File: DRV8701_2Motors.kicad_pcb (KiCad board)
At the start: 4 copper layers, 100 x 40 mm, 99 parts, among them J1 Conn_01x02, J12 Conn_01x02, J13 Conn_01x02, J2 Conn_01x10, J3 Conn_01x10, J6 Conn_01x04, J7 Conn_ST_STDC14, J8 Conn_01x04, J9 Conn_01x04, SW1 SW_SPDT_321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

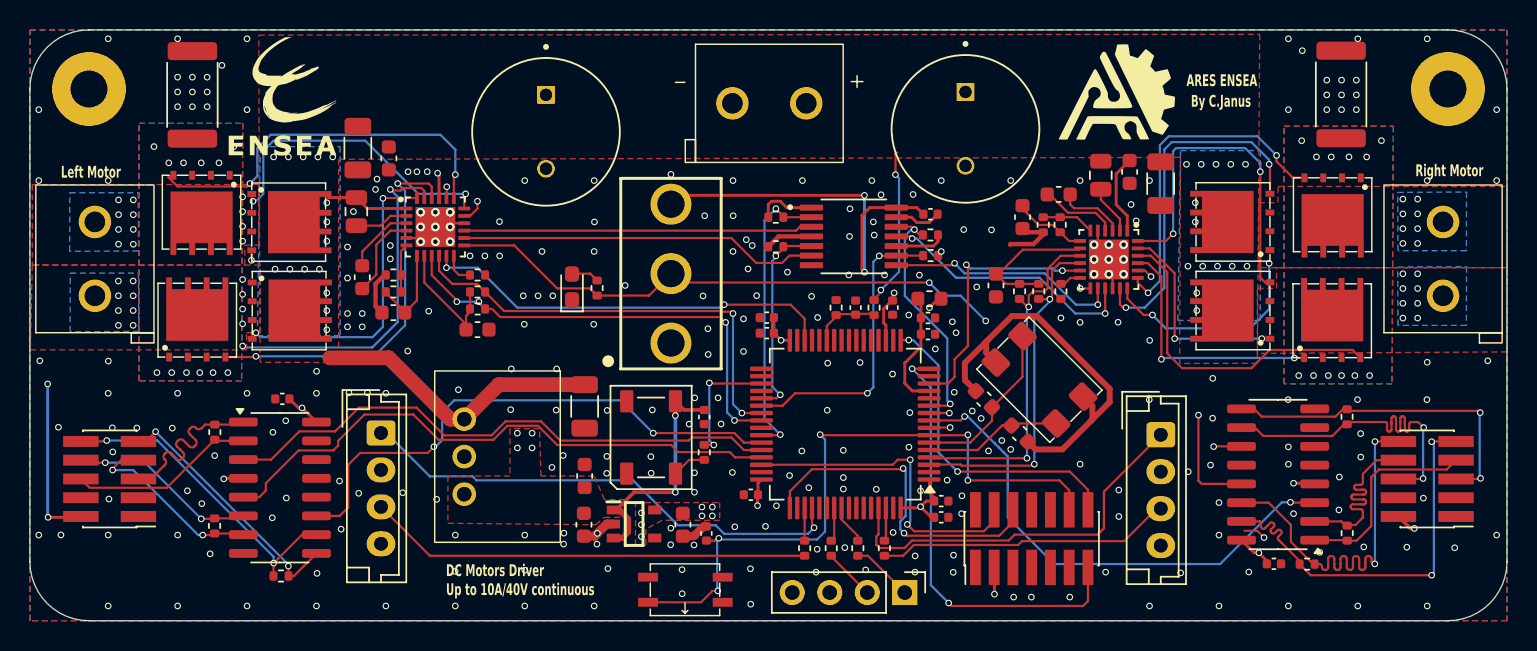
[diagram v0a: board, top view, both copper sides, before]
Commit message: alignement connecteur, changement connecteur
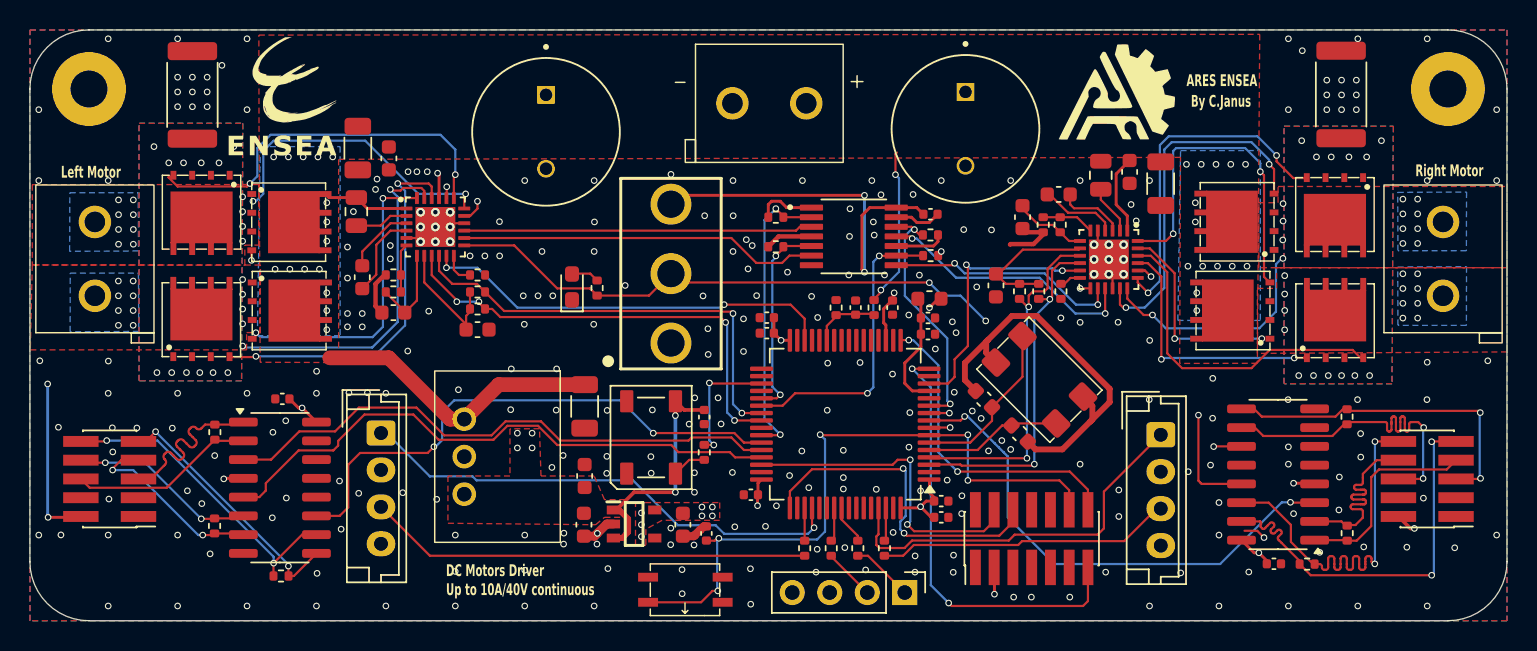
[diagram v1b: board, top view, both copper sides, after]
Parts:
- moved U21 0.28 mm to (85.6, 84.3)
- moved U24 0.28 mm to (155.4, 78.0)
- moved U20 0.20 mm to (162.4, 84.3)
- moved U22 0.16 mm to (162.3, 77.8)
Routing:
- net /MoteurDroit/SH1: track 14.8 -> 15.9 mm, vias 10 -> 13
- net /MoteurDroit/SH2: vias 10 -> 14
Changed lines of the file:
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@@
 	(footprint "TPH1R403NL:TPH1R403NL"
 		(layer "F.Cu")
-		(at 155.1 78 -90)
+		(at 155.38 77.99 -90)
 		(property "Reference" "U24"
 			(at -0.035 -6 270)
@@
 	(footprint "TPH1R403NL:TPH1R403NL"
 		(layer "F.Cu")
-		(at 85.33 84.3 180)
+		(at 85.61 84.27 180)
 		(property "Reference" "U21"
 			(at -0.035 -6 180)
@@
 	(footprint "TPH1R403NL:TPH1R403NL"
 		(layer "F.Cu")
-		(at 162.195 77.865)
+		(at 162.35 77.85)
 		(property "Reference" "U22"
 			(at -0.035 -6 0)
@@
 	(footprint "TPH1R403NL:TPH1R403NL"
 		(layer "F.Cu")
-		(at 162.165 84.34 180)
+		(at 162.36 84.34 180)
 		(property "Reference" "U20"
 			(at -0.035 -6 180)
@@
 	)
 	(segment
-		(start 157.3 81.77)
-		(end 157.625 82.095)
+		(start 151.4 78.8)
+		(end 150.91 79.29)
 		(width 0.15)
 		(layer "F.Cu")
@@
 	)
 	(segment
-		(start 157.625 82.095)
-		(end 157.95 82.095)
+		(start 157.3 74.6)
+		(end 157.55 74.85)
 		(width 0.15)
 		(layer "F.Cu")
@@
 	)
 	(segment
-		(start 151.4 78.8)
-		(end 150.91 79.29)
+		(start 157.55 74.85)
+		(end 157.55 81.72)
 		(width 0.15)
 		(layer "F.Cu")
@@
 	)
 	(segment
-		(start 157.3 74.6)
-		(end 157.3 81.77)
+		(start 157.925 82.095)
+		(end 157.95 82.095)
+		(width 0.15)
+		(layer "F.Cu")
+		(net 108)
+	)
+	(segment
+		(start 157.55 81.72)
+		(end 157.925 82.095)
 		(width 0.15)
 		(layer "F.Cu")
@@
 	)
 	(segment
-		(start 149.89 80.29)
-		(end 149 80.29)
+		(start 152 87.9)
+		(end 151 86.9)
 		(width 0.15)
 		(layer "F.Cu")
@@
 	)
 	(segment
-		(start 152 87.9)
-		(end 151 86.9)
+		(start 156.7 87.9)
+		(end 152 87.9)
 		(width 0.15)
 		(layer "F.Cu")
@@
 	)
 	(segment
+		(start 151 81.4)
+		(end 149.89 80.29)
+		(width 0.15)
+		(layer "F.Cu")
+		(net 109)
+	)
+	(segment
 		(start 163.544 86.664)
 		(end 157.936 86.664)
@@
 	)
 	(segment
-		(start 156.7 87.9)
-		(end 152 87.9)
+		(start 149.89 80.29)
+		(end 149 80.29)
 		(width 0.15)
 		(layer "F.Cu")
@@
 	)
 	(segment
-		(start 151 81.4)
-		(end 149.89 80.29)
+		(start 164.07 87.19)
+		(end 163.544 86.664)
 		(width 0.15)
 		(layer "F.Cu")
@@
 	)
 	(segment
-		(start 164.07 87.19)
-		(end 163.544 86.664)
+		(start 164.265 87.19)
+		(end 164.07 87.19)
 		(width 0.15)
 		(layer "F.Cu")
@@
 	)
 	(segment
+		(start 89.25 87.15)
+		(end 87.545 87.15)
+		(width 0.15)
+		(layer "F.Cu")
+		(net 110)
+	)
+	(segment
 		(start 101 75.4)
 		(end 101.2 75.6)
@@
 	)
 	(segment
-		(start 101.2 75.6)
-		(end 101.2 76.385)
+		(start 87.545 87.15)
+		(end 87.515 87.12)
 		(width 0.15)
 		(layer "F.Cu")
@@
 	)
 	(segment
-		(start 98.9 75.4)
-		(end 101 75.4)
+		(start 101.2 75.6)
+		(end 101.2 76.385)
 		(width 0.15)
 		(layer "F.Cu")
@@
 	)
 	(segment
-		(start 89.25 87.15)
-		(end 87.235 87.15)
+		(start 98.9 75.4)
+		(end 101 75.4)
 		(width 0.15)
 		(layer "F.Cu")
@@
 	)
 	(via
+		(at 158.84 77.94)
+		(size 0.45)
+		(drill 0.3)
+		(layers "F.Cu" "B.Cu")
+		(net 118)
+	)
+	(via
 		(at 167.950537 77.455726)
 		(size 0.45)
@@
 	)
 	(via
+		(at 158.84 76.76)
+		(size 0.45)
+		(drill 0.3)
+		(layers "F.Cu" "B.Cu")
+		(net 118)
+	)
+	(via
+		(at 158.82 79.22)
+		(size 0.45)
+		(drill 0.3)
+		(layers "F.Cu" "B.Cu")
+		(net 118)
+	)
+	(via
 		(at 167.950537 79.455726)
 		(size 0.45)
@@
 	)
 	(via
-		(at 157.9 80.8)
+		(at 158.83 80.47)
 		(size 0.45)
 		(drill 0.3)
@@
 	)
 	(segment
-		(start 150 84.3)
+		(start 158.83 80.47)
+		(end 158.75 80.47)
+		(width 0.15)
+		(layer "B.Cu")
+		(net 118)
+	)
+	(segment
+		(start 157.23 85.2)
 		(end 150.9 85.2)
 		(width 0.15)
@@
 	)
 	(segment
-		(start 150.9 85.2)
-		(end 156.6 85.2)
+		(start 158.75 80.47)
+		(end 158.36 80.86)
+		(width 0.15)
+		(layer "B.Cu")
+		(net 118)
+	)
+	(segment
+		(start 158.36 80.86)
+		(end 158.36 84.07)
 		(width 0.15)
 		(layer "B.Cu")
@@
 	)
 	(segment
-		(start 157.9 83.9)
-		(end 157.9 80.8)
+		(start 158.36 84.07)
+		(end 157.23 85.2)
 		(width 0.15)
 		(layer "B.Cu")
@@
 	)
 	(segment
-		(start 156.6 85.2)
-		(end 157.9 83.9)
+		(start 150.9 85.2)
+		(end 150 84.3)
 		(width 0.15)
 		(layer "B.Cu")
@@
 	)
 	(via
+		(at 158.95 82.88)
+		(size 0.45)
+		(drill 0.3)
+		(layers "F.Cu" "B.Cu")
+		(free yes)
+		(net 119)
+	)
+	(via
+		(at 158.95 81.64)
+		(size 0.45)
+		(drill 0.3)
+		(layers "F.Cu" "B.Cu")
+		(free yes)
+		(net 119)
+	)
+	(via
 		(at 166.950537 83.51)
 		(size 0.45)
@@
 	)
 	(via
+		(at 158.947463 85.303903)
+		(size 0.45)
+		(drill 0.3)
+		(layers "F.Cu" "B.Cu")
+		(free yes)
+		(net 119)
+	)
+	(via
+		(at 158.95 83.99)
+		(size 0.45)
+		(drill 0.3)
+		(layers "F.Cu" "B.Cu")
+		(free yes)
+		(net 119)
+	)
+	(via
 		(at 166.950537 81.51)
 		(size 0.45)
@@
 	)
 	(segment
-		(start 157.95 74.15)
-		(end 157.95 76.095)
-		(width 0.15)
-		(layer "F.Cu")
-		(net 122)
-	)
-	(segment
 		(start 148.01 83.8)
 		(end 147.795 83.585)
@@
 	(segment
 		(start 157.9 74.1)
-		(end 157.95 74.15)
+		(end 158.23 74.43)
+		(width 0.15)
+		(layer "F.Cu")
+		(net 122)
+	)
+	(segment
+		(start 158.23 74.43)
+		(end 158.23 76.085)
 		(width 0.15)
 		(layer "F.Cu")
@@
 	)
 	(segment
-		(start 160.245 75)
-		(end 160.275 75.03)
-		(width 0.15)
-		(layer "F.Cu")
-		(net 123)
-	)
-	(segment
-		(start 160.275 75)
-		(end 160.29 75.015)
-		(width 0.15)
-		(layer "F.Cu")
-		(net 123)
-	)
-	(segment
-		(start 158.4 73.9)
-		(end 159.5 75)
-		(width 0.15)
-		(layer "F.Cu")
-		(net 123)
-	)
-	(segment
-		(start 159.5 75)
-		(end 160.245 75)
+		(start 160.415 75.03)
+		(end 160.445 75)
 		(width 0.15)
 		(layer "F.Cu")
@@
 	)
 	(segment
-		(start 160.275 75.03)
-		(end 160.275 75)
+		(start 158.4 73.9)
+		(end 159.53 75.03)
+		(width 0.15)
+		(layer "F.Cu")
+		(net 123)
+	)
+	(segment
+		(start 159.53 75.03)
+		(end 160.415 75.03)
 		(width 0.15)
 		(layer "F.Cu")
@@
 	)
 	(segment
+		(start 160.24 87.21)
+		(end 160.26 87.19)
+		(width 0.15)
+		(layer "F.Cu")
+		(net 128)
+	)
+	(segment
 		(start 159.6 87.21)
 		(end 160.24 87.21)
@@
 	)
 	(segment
-		(start 160.24 87.21)
-		(end 160.26 87.19)
+		(start 160.26 87.19)
+		(end 160.455 87.19)
 		(width 0.15)
 		(layer "F.Cu")

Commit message: final push
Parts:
- removed SW1: SW_SPDT_321, switch:472121010111
- U10, U5: value ~ -> DRV8701
- U2: value ~ -> SN74HC125PWR
- moved R11 6.40 mm to (118.8, 82.5)
- moved D1 6.18 mm to (116.9, 82.4)
- moved C16 1.77 mm to (150.6, 73.6)
- moved C14 0.78 mm to (146.5, 74.1)
- moved C15 0.32 mm to (148.4, 74.3)
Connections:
- J7 pad 13: /STM_et_Osc/USART2_TX -> /STM_et_Osc/USART2_RX
- J7 pad 14: /STM_et_Osc/USART2_RX -> /STM_et_Osc/USART2_TX
- R11 pad 2: /nSLEEP -> /LED_state
- U16 pad 28: unconnected-(U16-PB2-Pad28) -> /nSLEEP
- U16 pad 29: unconnected-(U16-PB10-Pad29) -> /LED_state
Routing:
- net +3.3V: track 51.3 -> 32.8 mm, vias 19 -> 18
- net /LED_state: track 0.00 -> 10.5 mm
- net /STM_et_Osc/USART2_TX: track 30.0 -> 20.2 mm
- net /R_nFAULT: track 23.9 -> 33.0 mm, vias 2 -> 0
- net /R_SNSOUT: track 23.7 -> 31.5 mm
- net /nSLEEP: track 46.7 -> 50.6 mm
- net /STM_et_Osc/USART2_RX: track 21.7 -> 24.8 mm
- net GND: track 105.0 -> 106.5 mm, vias 284 -> 294
- net /R_ENCB: track 34.5 -> 33.4 mm
- net /STM_et_Osc/NRST: track 45.3 -> 44.4 mm
- net Net-(U5-VCP): track 3.33 -> 4.12 mm
- net /R_ENCI: track 26.4 -> 25.8 mm
- added copper zone on In2.Cu, net /MoteurDroit/SH1
- added copper zone on In2.Cu, net /MoteurDroit/SH2
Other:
- board text added: "STATE"

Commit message: last push
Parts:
- U17: footprint Oscillator:WE-XTAL Quartz Crystal 8MHz -> Crystal:Crystal_SMD_7050-4Pin_7.0x5.0mm
- moved G*** 3.96 mm to (151.6, 68.9)
- moved C33 0.36 mm to (140.7, 92.5)
- moved C32 0.31 mm to (138.5, 90.3)
- moved U17 0.28 mm to (142.5, 88.9)
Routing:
- net GND: track 106.5 -> 110.8 mm, vias 294 -> 297
- net /STM_et_Osc/Osc_IN: track 9.35 -> 12.3 mm
- net /STM_et_Osc/Osc_OUT: track 11.5 -> 8.76 mm

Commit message: last push
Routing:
- net GND: vias 297 -> 296
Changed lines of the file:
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@@
 	)
 	(via
-		(at 100.9 74.6)
-		(size 0.45)
-		(drill 0.3)
-		(layers "F.Cu" "B.Cu")
-		(free yes)
-		(net 1)
-	)
-	(via
 		(at 125.33 84.4)
 		(size 0.45)
@@
 	)
 	(segment
-		(start 101.6 74.7)
-		(end 101.7 74.8)
+		(start 101.7 75.41)
+		(end 101.7 76.385)
 		(width 0.2)
 		(layer "F.Cu")
@@
 	)
 	(segment
-		(start 101.7 74.8)
-		(end 101.7 76.385)
+		(start 101.36 75.07)
+		(end 101.7 75.41)
 		(width 0.2)
 		(layer "F.Cu")
@@
 	)
 	(via
-		(at 101.6 74.7)
+		(at 101.36 75.07)
 		(size 0.45)
 		(drill 0.3)
@@
 	)
 	(segment
-		(start 101.6 74.7)
-		(end 101.6 74.4)
+		(start 101.36 75.07)
+		(end 101.36 74.65)
 		(width 0.25)
 		(layer "In2.Cu")
@@
 	)
 	(segment
-		(start 100.1 72.9)
-		(end 87.8 72.9)
+		(start 101.36 74.65)
+		(end 99.61 72.9)
 		(width 0.25)
 		(layer "In2.Cu")
@@
 	)
 	(segment
-		(start 101.6 74.4)
-		(end 100.1 72.9)
+		(start 99.61 72.9)
+		(end 87.8 72.9)
 		(width 0.25)
 		(layer "In2.Cu")
